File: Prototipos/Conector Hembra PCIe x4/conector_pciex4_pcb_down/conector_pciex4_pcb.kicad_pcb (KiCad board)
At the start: 2 copper layers, 16.9 x 40.4 mm, 33 parts, among them J1 10018783-10211TLF

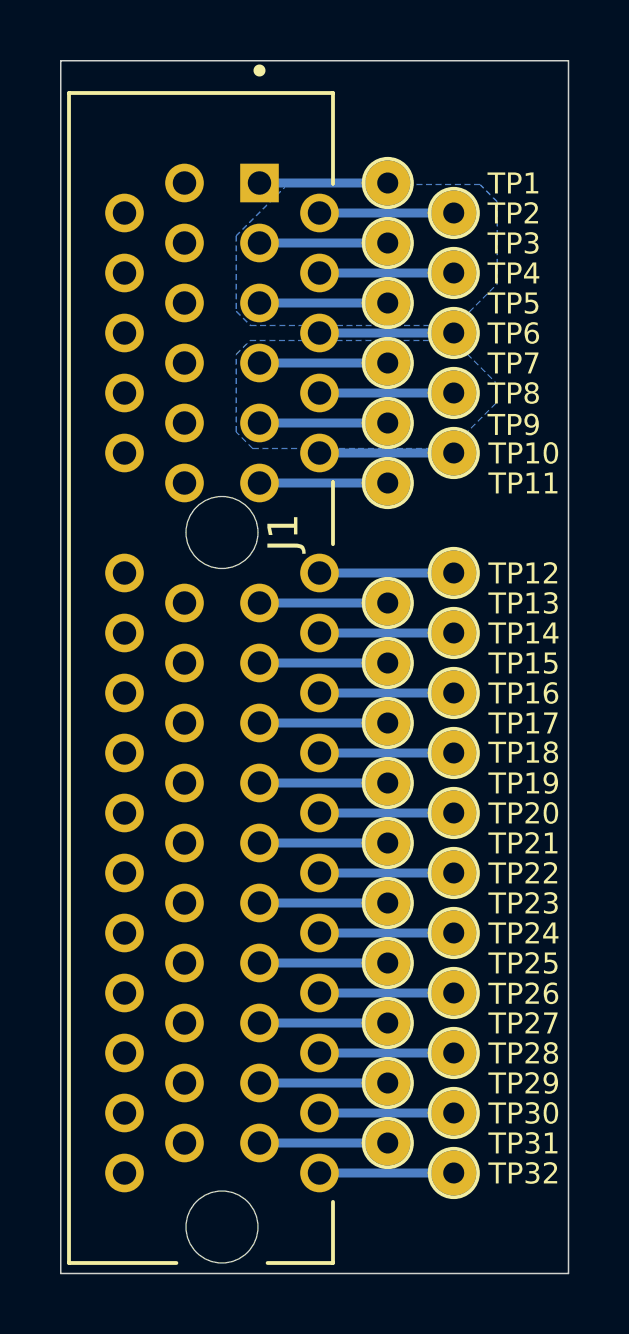
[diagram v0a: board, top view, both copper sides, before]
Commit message: Agregado de otra configuración de pines
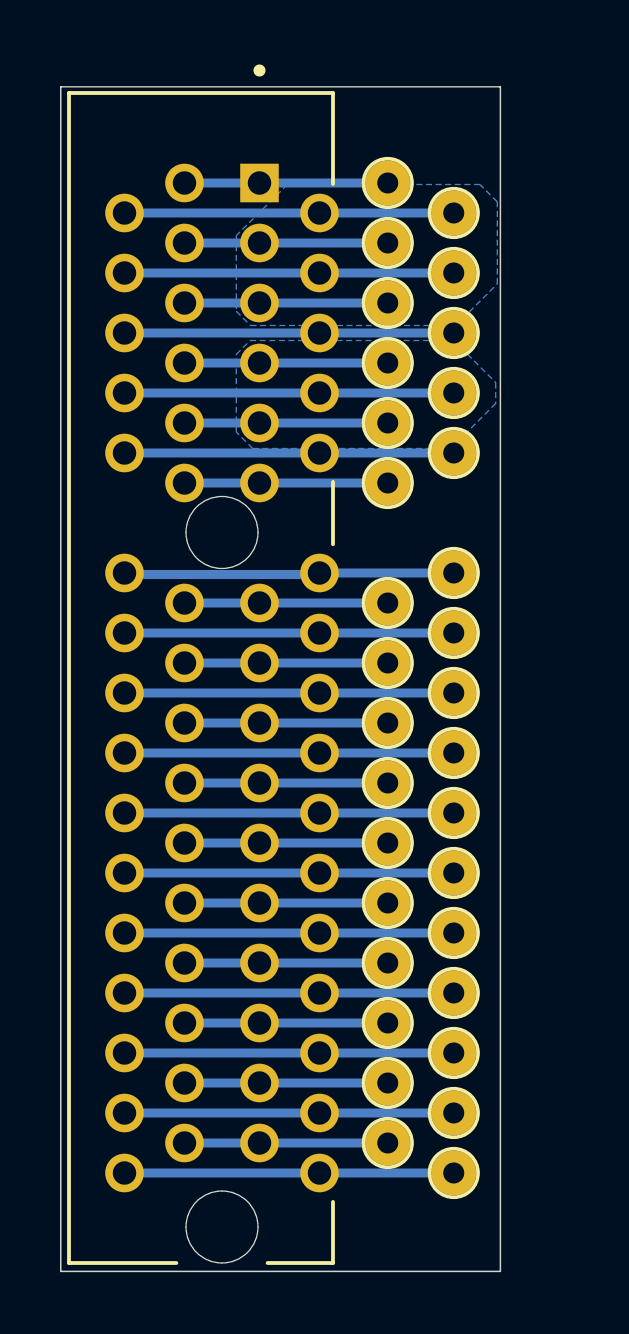
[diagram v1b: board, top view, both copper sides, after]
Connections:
- J1 pad B1: unconnected-(J1-PadB1) -> Net-(J1-PadA1)
- J1 pad B10: unconnected-(J1-PadB10) -> Net-(J1-PadA10)
- J1 pad B11: unconnected-(J1-PadB11) -> Net-(J1-PadA11)
- J1 pad B12: unconnected-(J1-PadB12) -> Net-(J1-PadA12)
- J1 pad B13: unconnected-(J1-PadB13) -> Net-(J1-PadA13)
- J1 pad B14: unconnected-(J1-PadB14) -> Net-(J1-PadA14)
- J1 pad B15: unconnected-(J1-PadB15) -> Net-(J1-PadA15)
- J1 pad B16: unconnected-(J1-PadB16) -> Net-(J1-PadA16)
- J1 pad B17: unconnected-(J1-PadB17) -> Net-(J1-PadA17)
- J1 pad B18: unconnected-(J1-PadB18) -> Net-(J1-PadA18)
- J1 pad B19: unconnected-(J1-PadB19) -> Net-(J1-PadA19)
- J1 pad B2: unconnected-(J1-PadB2) -> Net-(J1-PadA2)
- J1 pad B20: unconnected-(J1-PadB20) -> Net-(J1-PadA20)
- J1 pad B21: unconnected-(J1-PadB21) -> Net-(J1-PadA21)
- J1 pad B22: unconnected-(J1-PadB22) -> Net-(J1-PadA22)
- J1 pad B23: unconnected-(J1-PadB23) -> Net-(J1-PadA23)
- J1 pad B24: unconnected-(J1-PadB24) -> Net-(J1-PadA24)
- J1 pad B25: unconnected-(J1-PadB25) -> Net-(J1-PadA25)
- J1 pad B26: unconnected-(J1-PadB26) -> Net-(J1-PadA26)
- J1 pad B27: unconnected-(J1-PadB27) -> Net-(J1-PadA27)
- J1 pad B28: unconnected-(J1-PadB28) -> Net-(J1-PadA28)
- J1 pad B29: unconnected-(J1-PadB29) -> Net-(J1-PadA29)
- J1 pad B3: unconnected-(J1-PadB3) -> Net-(J1-PadA2)
- J1 pad B30: unconnected-(J1-PadB30) -> Net-(J1-PadA30)
- J1 pad B31: unconnected-(J1-PadB31) -> Net-(J1-PadA31)
- J1 pad B32: unconnected-(J1-PadB32) -> Net-(J1-PadA32)
- J1 pad B4: unconnected-(J1-PadB4) -> Net-(J1-PadA2)
- J1 pad B5: unconnected-(J1-PadB5) -> Net-(J1-PadA2)
- J1 pad B6: unconnected-(J1-PadB6) -> Net-(J1-PadA6)
- J1 pad B7: unconnected-(J1-PadB7) -> Net-(J1-PadA7)
- J1 pad B8: unconnected-(J1-PadB8) -> Net-(J1-PadA7)
- J1 pad B9: unconnected-(J1-PadB9) -> Net-(J1-PadA7)
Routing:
- net Net-(J1-PadA2): track 17.5 -> 35.5 mm
- net Net-(J1-PadA7): track 13.0 -> 24.5 mm
- net Net-(J1-PadA12): track 4.48 -> 11.0 mm
- net Net-(J1-PadA6): track 4.48 -> 11.0 mm
- net Net-(J1-PadA32): track 4.48 -> 11.0 mm
- net Net-(J1-PadA30): track 4.48 -> 11.0 mm
- net Net-(J1-PadA28): track 4.48 -> 11.0 mm
- net Net-(J1-PadA26): track 4.48 -> 11.0 mm
- net Net-(J1-PadA24): track 4.48 -> 11.0 mm
- net Net-(J1-PadA22): track 4.48 -> 11.0 mm
- net Net-(J1-PadA20): track 4.48 -> 11.0 mm
- net Net-(J1-PadA18): track 4.48 -> 11.0 mm
- net Net-(J1-PadA16): track 4.48 -> 11.0 mm
- net Net-(J1-PadA14): track 4.48 -> 11.0 mm
- net Net-(J1-PadA10): track 4.48 -> 11.0 mm
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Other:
- board size 16.9 x 40.4 mm -> 14.7 x 39.5 mm
